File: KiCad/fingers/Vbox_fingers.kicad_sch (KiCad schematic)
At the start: 4 parts, among them J1 Conn_01x06, J2 Conn_01x06, J6 Conn_01x10, J7 Conn_01x10

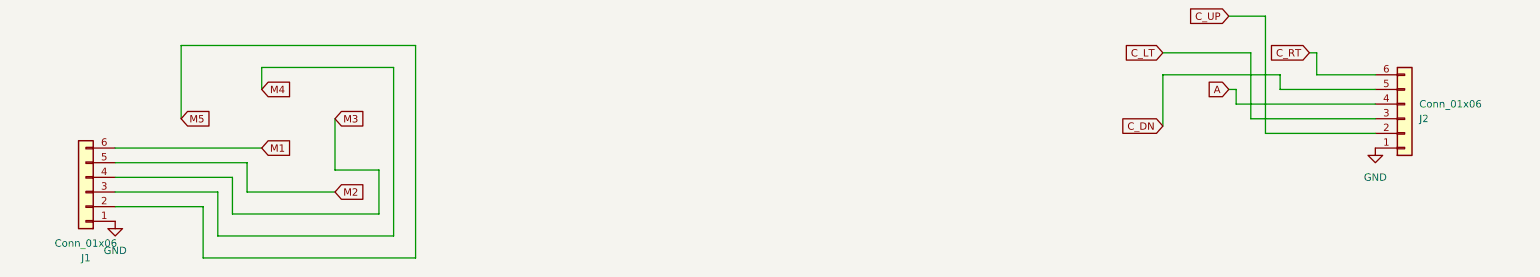
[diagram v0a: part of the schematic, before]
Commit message: framework for button clusters
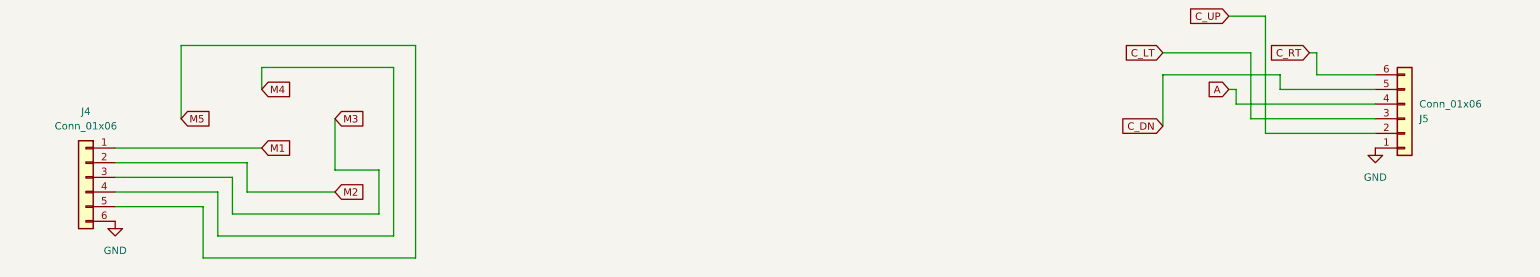
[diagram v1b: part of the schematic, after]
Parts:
- removed J1, J2: Conn_01x06, Connector_JST:JST_PH_S6B-PH-SM4-TB_1x06-1MP_P2.00mm_Horizontal, symbol Connector_Generic:Conn_01x06
- added J4, J5: Conn_01x06, Connector_JST:JST_PH_S6B-PH-SM4-TB_1x06-1MP_P2.00mm_Horizontal, symbol Connector_Generic:Conn_01x06
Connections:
- net A: now also J5.4 (Pin_4)
- net C_DN: now also J5.5 (Pin_5)
- net C_LT: now also J5.3 (Pin_3)
- net C_RT: now also J5.6 (Pin_6)
- net C_UP: now also J5.2 (Pin_2)
- net GND: now also J4.6 (Pin_6), J5.1 (Pin_1)
- net M1: now also J4.1 (Pin_1)
- net M2: now also J4.2 (Pin_2)
- net M3: now also J4.3 (Pin_3)
- net M4: now also J4.4 (Pin_4)
- net M5: now also J4.5 (Pin_5)
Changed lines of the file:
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@@
+    )
+  )
+  (symbol (lib_id "Connector_Generic:Conn_01x06") (at 27.94 156.21 0) (mirror y) (unit 1)
+    (in_bom yes) (on_board yes) (dnp no)
+    (property "Reference" "J4" (at 27.94 144.78 0)
+      (effects (font (size 1.27 1.27)))
+    )
+    (property "Value" "Conn_01x06" (at 27.94 147.32 0)
+      (effects (font (size 1.27 1.27)))
+    )
+    (property "Footprint" "Connector_JST:JST_PH_S6B-PH-SM4-TB_1x06-1MP_P2.00mm_Horizontal" (at 27.94 156.21 0)
+      (effects (font (size 1.27 1.27)) hide)
+    )
+    (property "Datasheet" "~" (at 27.94 156.21 0)
+      (effects (font (size 1.27 1.27)) hide)
+    )
+    (pin "1")
+    (pin "2")
+    (pin "3")
+    (pin "4")
+    (pin "5")
+    (pin "6")
+    (instances
+      (project "Vbox_thumbs"
+        (path "/9f19960e-6523-4fd2-955a-272ad4648acf"
+          (reference "J4") (unit 1)
+        )
+      )
+    )
+  )
+  (symbol (lib_id "Connector_Generic:Conn_01x06") (at 256.54 146.05 0) (mirror x) (unit 1)
+    (in_bom yes) (on_board yes) (dnp no)
+    (property "Reference" "J5" (at 259.08 146.05 0)
+      (effects (font (size 1.27 1.27)) (justify left))
+    )
+    (property "Value" "Conn_01x06" (at 259.08 143.51 0)
+      (effects (font (size 1.27 1.27)) (justify left))
+    )
+    (property "Footprint" "Connector_JST:JST_PH_S6B-PH-SM4-TB_1x06-1MP_P2.00mm_Horizontal" (at 256.54 146.05 0)
+      (effects (font (size 1.27 1.27)) hide)
+    )
+    (property "Datasheet" "~" (at 256.54 146.05 0)
+      (effects (font (size 1.27 1.27)) hide)
+    )
+    (pin "1")
+    (pin "2")
+    (pin "3")
+    (pin "4")
+    (pin "5")
+    (pin "6")
+    (instances
+      (project "Vbox_thumbs"
+        (path "/9f19960e-6523-4fd2-955a-272ad4648acf"
+          (reference "J5") (unit 1)
+        )
+      )
     )
   )
@@
     )
   )
-  (symbol (lib_id "Connector_Generic:Conn_01x06") (at 256.54 146.05 0) (mirror x) (unit 1)
-    (in_bom yes) (on_board yes) (dnp no)
-    (property "Reference" "J2" (at 259.08 146.05 0)
-      (effects (font (size 1.27 1.27)) (justify left))
-    )
-    (property "Value" "Conn_01x06" (at 259.08 143.51 0)
-      (effects (font (size 1.27 1.27)) (justify left))
-    )
-    (property "Footprint" "Connector_JST:JST_PH_S6B-PH-SM4-TB_1x06-1MP_P2.00mm_Horizontal" (at 256.54 146.05 0)
-      (effects (font (size 1.27 1.27)) hide)
-    )
-    (property "Datasheet" "~" (at 256.54 146.05 0)
-      (effects (font (size 1.27 1.27)) hide)
-    )
-    (pin "1")
-    (pin "2")
-    (pin "3")
-    (pin "4")
-    (pin "5")
-    (pin "6")
-    (instances
-      (project "Vbox_thumbs"
-        (path "/9f19960e-6523-4fd2-955a-272ad4648acf"
-          (reference "J2") (unit 1)
-        )
-      )
-    )
-  )
   (symbol (lib_id "Connector_Generic:Conn_01x10") (at 21.59 38.1 0) (mirror y) (unit 1)
     (in_bom yes) (on_board yes) (dnp no) (fields_autoplaced)
@@
         )
       )
-    )
-  )
-  (symbol (lib_id "Connector_Generic:Conn_01x06") (at 27.94 158.75 180) (unit 1)
-    (in_bom yes) (on_board yes) (dnp no)
-    (property "Reference" "J1" (at 27.94 170.18 0)
-      (effects (font (size 1.27 1.27)))
-    )
-    (property "Value" "Conn_01x06" (at 27.94 167.64 0)
-      (effects (font (size 1.27 1.27)))
-    )
-    (property "Footprint" "Connector_JST:JST_PH_S6B-PH-SM4-TB_1x06-1MP_P2.00mm_Horizontal" (at 27.94 158.75 0)
-      (effects (font (size 1.27 1.27)) hide)
-    )
-    (property "Datasheet" "~" (at 27.94 158.75 0)
-      (effects (font (size 1.27 1.27)) hide)
-    )
-    (pin "1")
-    (pin "2")
-    (pin "3")
-    (pin "4")
-    (pin "5")
-    (pin "6")
-    (instances
-      (project "Vbox_thumbs"
-        (path "/9f19960e-6523-4fd2-955a-272ad4648acf"
-          (reference "J1") (unit 1)
-        )
-      )

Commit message: thumbs and fingers
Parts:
- removed J4, J5: Conn_01x06, Connector_JST:JST_PH_S6B-PH-SM4-TB_1x06-1MP_P2.00mm_Horizontal, symbol Connector_Generic:Conn_01x06
- removed J6, J7: Conn_01x10, Connector_JST:JST_PH_S10B-PH-SM4-TB_1x10-1MP_P2.00mm_Horizontal, symbol Connector_Generic:Conn_01x10
- added J1, J2: Conn_01x10, Connector_JST:JST_PH_S10B-PH-SM4-TB_1x10-1MP_P2.00mm_Horizontal, symbol Connector_Generic:Conn_01x10
- added SW1, SW10, SW11, SW12, SW13, SW14, SW15, SW16, SW17, SW18, SW2, SW3, SW4, SW5, SW6, SW7, SW8, SW9: SW_Push_45deg, Buttons:Vbox, symbol Switch:SW_Push_45deg
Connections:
- net B: now also J2.3 (Pin_3), SW18.1
- net DOWN: now also J1.7 (Pin_7), SW8.1
- net GND: now also J1.1 (Pin_1), J2.10 (Pin_10)
- net INDEX2: now also J1.2 (Pin_2), SW4.1
- net L: now also J1.5 (Pin_5), SW6.1
- net LEFT: now also J1.6 (Pin_6), SW7.1
- net LS: now also J2.6 (Pin_6), SW11.1
- net MS: now also J2.8 (Pin_8), SW10.1
- net PINKY2: now also J1.4 (Pin_4), SW1.1
- net R: now also J2.2 (Pin_2), SW13.1
- net RIGHT: now also J1.8 (Pin_8), SW9.1
- net RIGHTSTART: now also J2.1 (Pin_1), SW14.1
- net RING2: now also J1.3 (Pin_3), SW2.1
- net START: now also J1.10 (Pin_10), SW5.1
- net UP: now also J2.9 (Pin_9), SW15.1
- net UP2: now also J1.9 (Pin_9), SW3.1
- net X: now also J2.5 (Pin_5), SW17.1
- net Y: now also J2.4 (Pin_4), SW12.1
- net Z: now also J2.7 (Pin_7), SW16.1

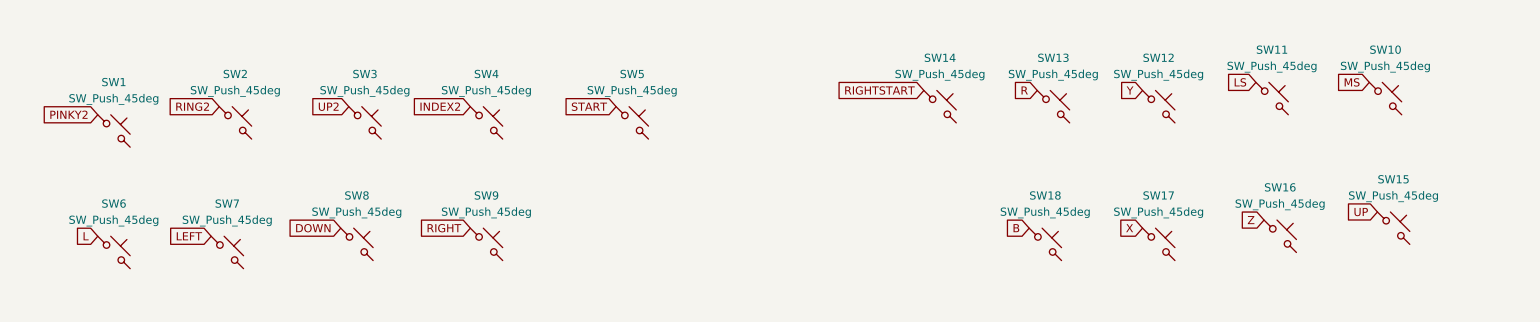
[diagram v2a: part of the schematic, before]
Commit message: add thermal clearances to fingers, a few more vias
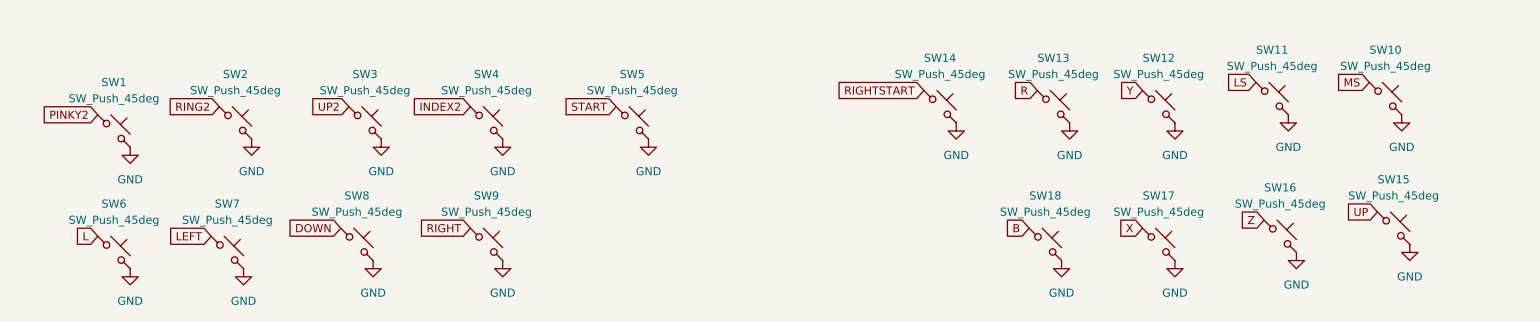
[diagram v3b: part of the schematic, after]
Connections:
- net GND: now also SW1.2, SW10.2, SW11.2, SW12.2, SW13.2, SW14.2, SW15.2, SW16.2, SW17.2, SW18.2, SW2.2, SW3.2, SW4.2, SW5.2, SW6.2, SW7.2, SW8.2, SW9.2

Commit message: make both sides share holes
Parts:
- SW10, SW11, SW12, SW13, SW14, SW15, SW16, SW17, SW18: footprint Buttons:Vbox -> Buttons:Vbox_1
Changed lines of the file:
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@@
       (effects (font (size 1.27 1.27)))
     )
-    (property "Footprint" "Buttons:Vbox" (at 168.91 76.2 0)
+    (property "Footprint" "Buttons:Vbox_1" (at 168.91 76.2 0)
       (effects (font (size 1.27 1.27)) hide)
     )
@@
       (effects (font (size 1.27 1.27)))
     )
-    (property "Footprint" "Buttons:Vbox" (at 240.03 95.25 0)
+    (property "Footprint" "Buttons:Vbox_1" (at 240.03 95.25 0)
       (effects (font (size 1.27 1.27)) hide)
     )
@@
       (effects (font (size 1.27 1.27)))
     )
-    (property "Footprint" "Buttons:Vbox" (at 222.25 96.52 0)
+    (property "Footprint" "Buttons:Vbox_1" (at 222.25 96.52 0)
       (effects (font (size 1.27 1.27)) hide)
     )
@@
       (effects (font (size 1.27 1.27)))
     )
-    (property "Footprint" "Buttons:Vbox" (at 220.98 74.93 0)
+    (property "Footprint" "Buttons:Vbox_1" (at 220.98 74.93 0)
       (effects (font (size 1.27 1.27)) hide)
     )
@@
       (effects (font (size 1.27 1.27)))
     )
-    (property "Footprint" "Buttons:Vbox" (at 203.2 76.2 0)
+    (property "Footprint" "Buttons:Vbox_1" (at 203.2 76.2 0)
       (effects (font (size 1.27 1.27)) hide)
     )
@@
       (effects (font (size 1.27 1.27)))
     )
-    (property "Footprint" "Buttons:Vbox" (at 185.42 97.79 0)
+    (property "Footprint" "Buttons:Vbox_1" (at 185.42 97.79 0)
       (effects (font (size 1.27 1.27)) hide)
     )
@@
       (effects (font (size 1.27 1.27)))
     )
-    (property "Footprint" "Buttons:Vbox" (at 186.69 76.2 0)
+    (property "Footprint" "Buttons:Vbox_1" (at 186.69 76.2 0)
       (effects (font (size 1.27 1.27)) hide)
     )
@@
       (effects (font (size 1.27 1.27)))
     )
-    (property "Footprint" "Buttons:Vbox" (at 238.76 74.93 0)
+    (property "Footprint" "Buttons:Vbox_1" (at 238.76 74.93 0)
       (effects (font (size 1.27 1.27)) hide)
     )
@@
       (effects (font (size 1.27 1.27)))
     )
-    (property "Footprint" "Buttons:Vbox" (at 203.2 97.79 0)
-      (effects (font (size 1.27 1.27)) hide)
-    )
+    (property "Footprint" "Buttons:Vbox_1" (at 203.2 97.79 0)
+      (effects (font (size 1.27 1.27)) hide)
+    )

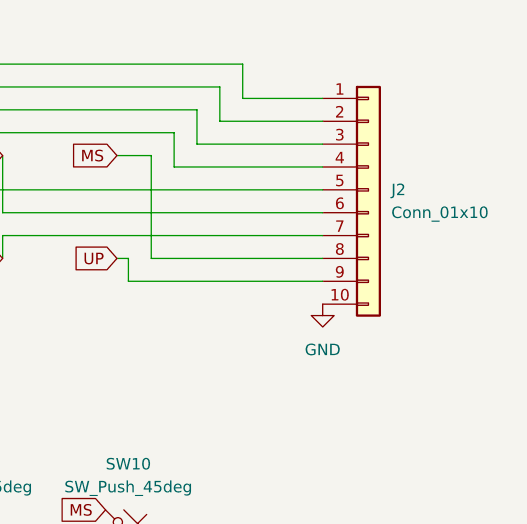
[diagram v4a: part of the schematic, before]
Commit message: flip connectors
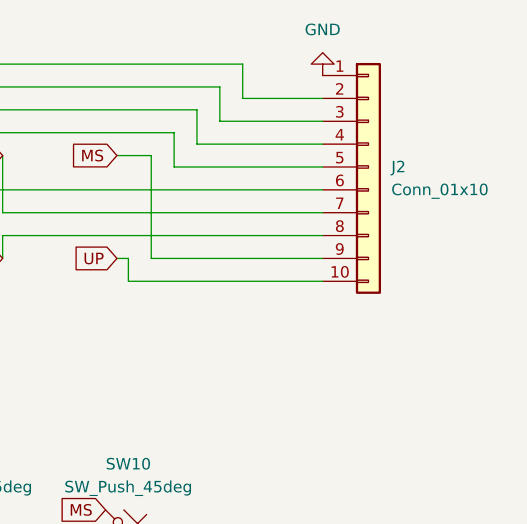
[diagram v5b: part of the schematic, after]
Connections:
- net B: now also J2.4 (Pin_4); no longer J2.3 (Pin_3)
- net GND: now also J2.1 (Pin_1); no longer J2.10 (Pin_10)
- net LS: now also J2.7 (Pin_7); no longer J2.6 (Pin_6)
- net MS: now also J2.9 (Pin_9); no longer J2.8 (Pin_8)
- net R: now also J2.3 (Pin_3); no longer J2.2 (Pin_2)
- net RIGHTSTART: now also J2.2 (Pin_2); no longer J2.1 (Pin_1)
- net UP: now also J2.10 (Pin_10); no longer J2.9 (Pin_9)
- net X: now also J2.6 (Pin_6); no longer J2.5 (Pin_5)
- net Y: now also J2.5 (Pin_5); no longer J2.4 (Pin_4)
- net Z: now also J2.8 (Pin_8); no longer J2.7 (Pin_7)
